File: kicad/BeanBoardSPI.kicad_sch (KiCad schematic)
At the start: 40 parts, among them J1 Power, J10 SPI6, J11 GPO, J12 GPO, J13 GPI, J14 GPI, J15 Power, J2 Address, J3 Data / Control, J4 SPI0 (RA8875), J5 SPI1, J6 SPI2, J7 SPI3, J8 SPI4, J9 SPI5, U1 74HC244, U10 74HC138, U11 74HC165, U12 74HC244, U13 74HC02, U2 74HC164, U3 74HC165, U4 74HC373, U5 74HC165, U6 74HC165, U8 74HC02, U9 74HC74

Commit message: schematic
tidy footprints  symbols
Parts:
- J1: value Power -> Conn_01x03_Pin
- J12: value GPO -> Conn_01x10_Pin
- J13: value GPI -> Conn_01x10_Pin
- J2: value Address -> Conn_01x16_Pin
- J3: value Data / Control -> Conn_01x16_Pin
- JP1: value CLK -> Jumper_2_Open; symbol Jumper:Jumper_2_Open -> PinHeader_Jumper:Jumper_2_Open
- JP2: value CLK/2 -> Jumper_2_Open; symbol Jumper:Jumper_2_Open -> PinHeader_Jumper:Jumper_2_Open
- JP3: symbol Jumper:Jumper_2_Bridged -> PinHeader_Jumper:Jumper_2_Bridged
- U1, U12: footprint (none) -> Package_DIP:DIP-20_W7.62mm
- U11, U3, U5, U6: footprint (none) -> Package_DIP:DIP-16_W7.62mm
- U13, U2: footprint (none) -> Package_DIP:DIP-14_W7.62mm_Socket
- U8: renamed from U13; footprint (none) -> Package_DIP:DIP-14_W7.62mm_Socket
- renumbered U8 to U13
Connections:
- net CTRL_WR: now also U13.10; no longer U13.13
- net INT_CLK: now also U13.12; no longer U13.3
- net SER_CLK: now also U13.13; no longer U13.1
- net ~{DATA_RD}: now also U8.4; no longer U8.10
- net ~{RD}: now also U8.2; no longer U8.5
- net ~{SER_EN}: now also U13.11; no longer U13.2
- net ~{WR}: now also U13.8; no longer U13.11
- net at U10.10 (~{Y5}), U8.8: now also U8.3; no longer U8.6
- net at U10.11 (~{Y4}), U13.3: now also U13.9; no longer U13.12
- new net: U8.1, U8.5, U8.6
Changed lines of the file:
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@@
 		(lib_id "74xx:74HC02")
 		(at 87.63 107.95 0)
-		(unit 2)
+		(unit 1)
 		(body_style 1)
 		(exclude_from_sim no)
@@
 				(path "/6c08ad2a-e233-4d4c-8add-9bc0e49a4487"
 					(reference "U8")
-					(unit 2)
+					(unit 1)
 				)
 			)
@@
 		(lib_id "74xx:74HC02")
 		(at 102.87 107.95 0)
-		(unit 3)
+		(unit 2)
 		(body_style 1)
 		(exclude_from_sim no)
@@
 		(in_pos_files yes)
 		(dnp no)
-		(fields_autoplaced yes)
-		(property "Reference" "U13"
-			(at 102.87 99.06 0)
+		(property "Reference" "U8"
+			(at 102.87 107.95 0)
 			(show_name no)
 			(do_not_autoplace no)
@@
 			)
 		)
-		(property "Footprint" ""
+		(property "Footprint" "Package_DIP:DIP-14_W7.62mm_Socket"
 			(at 102.87 107.95 0)
 			(hide yes)
@@
 			(project "BeanBoardSPI"
 				(path "/6c08ad2a-e233-4d4c-8add-9bc0e49a4487"
-					(reference "U13")
-					(unit 3)
+					(reference "U8")
+					(unit 2)
 				)
 			)
@@
 	)
 	(symbol
-		(lib_id "Jumper:Jumper_2_Open")
+		(lib_id "PinHeader_Jumper:Jumper_2_Open")
 		(at 163.83 149.86 0)
 		(unit 1)
@@
 		(dnp no)
 		(property "Reference" "JP1"
-			(at 163.6527 146.4748 0)
+			(at 163.83 147.066 0)
 			(show_name no)
 			(do_not_autoplace no)
@@
 			)
 		)
-		(property "Value" "CLK"
-			(at 163.83 146.05 0)
+		(property "Value" "Jumper_2_Open"
+			(at 163.83 152.146 0)
 			(hide yes)
 			(show_name no)
@@
 			)
 		)
-		(property "Description" ""
+		(property "Description" "Jumper, 2-pole, open"
 			(at 163.83 149.86 0)
+			(hide yes)
 			(show_name no)
 			(do_not_autoplace no)
@@
 			)
 		)
-		(property "Footprint" ""
+		(property "Footprint" "Package_DIP:DIP-16_W7.62mm"
 			(at 275.59 97.79 0)
 			(hide yes)
@@
 			)
 		)
-		(property "Footprint" ""
+		(property "Footprint" "Package_DIP:DIP-20_W7.62mm"
 			(at 223.52 95.25 0)
 			(hide yes)
@@
 			)
 		)
-		(property "Footprint" ""
+		(property "Footprint" "Package_DIP:DIP-16_W7.62mm"
 			(at 332.74 152.4 0)
 			(hide yes)
@@
 			)
 		)
-		(property "Footprint" ""
+		(property "Footprint" "Package_DIP:DIP-14_W7.62mm_Socket"
 			(at 11.43 160.02 0)
 			(hide yes)
@@
 		(in_pos_files yes)
 		(dnp no)
-		(fields_autoplaced yes)
 		(property "Reference" "U13"
-			(at 99.06 69.85 0)
+			(at 99.314 78.74 0)
 			(show_name no)
 			(do_not_autoplace no)
@@
 		(property "Value" "74HC02"
 			(at 99.06 72.39 0)
+			(hide yes)
 			(show_name no)
 			(do_not_autoplace no)
@@
 			)
 		)
-		(property "Footprint" ""
+		(property "Footprint" "Package_DIP:DIP-14_W7.62mm_Socket"
 			(at 99.06 78.74 0)
 			(hide yes)
@@
 			)
 		)
-		(property "Value" "Power"
+		(property "Value" "Conn_01x03_Pin"
 			(at 76.2 6.35 0)
+			(hide yes)
 			(show_name no)
 			(do_not_autoplace no)
@@
 			)
 		)
-		(property "Description" ""
+		(property "Description" "Generic connector, single row, 01x03, script generated"
 			(at 73.66 13.97 0)
+			(hide yes)
 			(show_name no)
 			(do_not_autoplace no)
@@
 		(in_pos_files yes)
 		(dnp no)
-		(fields_autoplaced yes)
 		(property "Reference" "U13"
-			(at 83.82 69.85 0)
+			(at 84.328 78.74 0)
 			(show_name no)
 			(do_not_autoplace no)
@@
 		(property "Value" "74HC02"
 			(at 83.82 72.39 0)
+			(hide yes)
 			(show_name no)
 			(do_not_autoplace no)
@@
 			)
 		)
-		(property "Footprint" ""
+		(property "Footprint" "Package_DIP:DIP-14_W7.62mm_Socket"
 			(at 83.82 78.74 0)
 			(hide yes)
@@
 		(in_pos_files yes)
 		(dnp no)
-		(fields_autoplaced yes)
-		(property "Reference" "U13"
-			(at 101.6 115.57 0)
+		(property "Reference" "U8"
+			(at 101.854 124.46 0)
 			(show_name no)
 			(do_not_autoplace no)
@@
 		(property "Value" "74HC02"
 			(at 101.6 118.11 0)
+			(hide yes)
 			(show_name no)
 			(do_not_autoplace no)
@@
 			)
 		)
-		(property "Footprint" ""
+		(property "Footprint" "Package_DIP:DIP-14_W7.62mm_Socket"
 			(at 101.6 124.46 0)
 			(hide yes)
@@
 			(project "BeanBoardSPI"
 				(path "/6c08ad2a-e233-4d4c-8add-9bc0e49a4487"
-					(reference "U13")
+					(reference "U8")
 					(unit 4)
 				)
@@
 			)
 		)
-		(property "Footprint" ""
+		(property "Footprint" "Package_DIP:DIP-14_W7.62mm_Socket"
 			(at 212.09 97.79 0)
 			(hide yes)
@@
 			)
 		)
-		(property "Footprint" ""
+		(property "Footprint" "Package_DIP:DIP-16_W7.62mm"
 			(at 332.74 97.79 0)
 			(hide yes)
@@
 		(lib_id "74xx:74HC02")
 		(at 93.98 90.17 0)
-		(unit 4)
+		(unit 3)
 		(body_style 1)
 		(exclude_from_sim no)
@@
 		(in_pos_files yes)
 		(dnp no)
-		(property "Reference" "U8"
+		(property "Reference" "U13"
 			(at 93.98 90.17 0)
 			(show_name no)
@@
 			(project "BeanBoardSPI"
 				(path "/6c08ad2a-e233-4d4c-8add-9bc0e49a4487"
-					(reference "U8")
-					(unit 4)
+					(reference "U13")
+					(unit 3)
 				)
 			)
@@
 	)
 	(symbol
-		(lib_id "Jumper:Jumper_2_Bridged")
+		(lib_id "PinHeader_Jumper:Jumper_2_Bridged")
 		(at 163.83 161.29 0)
 		(unit 1)
@@
 		(dnp no)
 		(property "Reference" "JP3"
-			(at 163.8593 159.3734 0)
+			(at 163.83 159.385 0)
 			(show_name no)
 			(do_not_autoplace no)
@@
 		)
 		(property "Value" "Jumper_2_Bridged"
-			(at 163.83 158.75 0)
+			(at 163.83 163.83 0)
 			(hide yes)
 			(show_name no)
@@
 		)
 		(property "Datasheet" ""
-			(at 163.83 161.29 0)
+			(at 163.83 166.37 0)
 			(hide yes)
 			(show_name no)
@@
 		)
 		(property "Description" "Jumper, 2-pole, closed/bridged"
-			(at 163.83 161.29 0)
+			(at 163.83 168.91 0)
 			(hide yes)
 			(show_name no)
@@
 			)
 		)
-		(property "Value" "Data / Control"
+		(property "Value" "Conn_01x16_Pin"
 			(at 55.88 8.89 0)
+			(hide yes)
 			(show_name no)
 			(do_not_autoplace no)
@@
 			)
 		)
-		(property "Description" ""
+		(property "Description" "Generic connector, single row, 01x16, script generated"
 			(at 55.88 31.75 0)
+			(hide yes)
 			(show_name no)
 			(do_not_autoplace no)
@@
 			)
 		)
-		(property "Footprint" ""
+		(property "Footprint" "Package_DIP:DIP-20_W7.62mm"
 			(at 223.52 146.05 0)
 			(hide yes)
@@
 		(lib_id "74xx:74HC02")
 		(at 176.53 142.24 0)
-		(unit 1)
+		(unit 4)
 		(body_style 1)
 		(exclude_from_sim no)
@@
 		(in_pos_files yes)
 		(dnp no)
-		(property "Reference" "U8"
+		(property "Reference" "U13"
 			(at 176.53 142.24 0)
 			(show_name no)
@@
 			(project "BeanBoardSPI"
 				(path "/6c08ad2a-e233-4d4c-8add-9bc0e49a4487"
-					(reference "U8")
-					(unit 1)
+					(reference "U13")
+					(unit 4)
 				)
 			)
@@
 			)
 		)
-		(property "Value" "GPO"
+		(property "Value" "Conn_01x10_Pin"
 			(at 74.93 24.13 0)
+			(hide yes)
 			(show_name no)
 			(do_not_autoplace no)
@@
 			)
 		)
-		(property "Description" ""
+		(property "Description" "Generic connector, single row, 01x10, script generated"
 			(at 73.66 38.1 0)
+			(hide yes)
 			(show_name no)
 			(do_not_autoplace no)
@@
 			)
 		)
-		(property "Value" "GPI"
+		(property "Value" "Conn_01x10_Pin"
 			(at 90.17 24.13 0)
+			(hide yes)
 			(show_name no)
 			(do_not_autoplace no)
@@
 			)
 		)
-		(property "Description" ""
+		(property "Description" "Generic connector, single row, 01x10, script generated"
 			(at 88.9 38.1 0)
+			(hide yes)
 			(show_name no)
 			(do_not_autoplace no)
@@
 			)
 		)
-		(property "Value" "Address"
+		(property "Value" "Conn_01x16_Pin"
 			(at 36.83 8.89 0)
+			(hide yes)
 			(show_name no)
 			(do_not_autoplace no)
@@
 			)
 		)
-		(property "Description" ""
+		(property "Description" "Generic connector, single row, 01x16, script generated"
 			(at 34.29 31.75 0)
+			(hide yes)
 			(show_name no)
 			(do_not_autoplace no)
@@
 	)
 	(symbol
-		(lib_id "Jumper:Jumper_2_Open")
+		(lib_id "PinHeader_Jumper:Jumper_2_Open")
 		(at 163.83 156.21 0)
 		(unit 1)
@@
 		(dnp no)
 		(property "Reference" "JP2"
-			(at 163.7904 153.2837 0)
+			(at 163.83 153.416 0)
 			(show_name no)
 			(do_not_autoplace no)
@@
 			)
 		)
-		(property "Value" "CLK/2"
-			(at 163.83 152.4 0)
+		(property "Value" "Jumper_2_Open"
+			(at 163.83 158.496 0)
 			(hide yes)
 			(show_name no)
@@
 			)
 		)
-		(property "Description" ""
+		(property "Description" "Jumper, 2-pole, open"
 			(at 163.83 156.21 0)
+			(hide yes)
 			(show_name no)
 			(do_not_autoplace no)
@@
 			)
 		)
-		(property "Footprint" ""
+		(property "Footprint" "Package_DIP:DIP-16_W7.62mm"
 			(at 275.59 152.4 0)
 			(hide yes)

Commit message: schematic
remove unused libraries
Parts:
- U1, U12: symbol 74xx:74HC244 -> 74HC244:74HC244
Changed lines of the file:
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@@
 	)
 	(symbol
-		(lib_id "74xx:74HC244")
+		(lib_id "74HC244:74HC244")
 		(at 223.52 95.25 0)
 		(unit 1)
@@
 		(dnp no)
 		(property "Reference" "U1"
-			(at 228.854 74.676 0)
-			(show_name no)
-			(do_not_autoplace no)
-			(effects
-				(font
-					(size 1.27 1.27)
-				)
-				(justify left)
+			(at 215.9 78.74 0)
+			(show_name no)
+			(do_not_autoplace no)
+			(effects
+				(font
+					(size 1.27 1.27)
+				)
 			)
 		)
 		(property "Value" "74HC244"
-			(at 225.6633 77.47 0)
-			(show_name no)
-			(do_not_autoplace no)
-			(effects
-				(font
-					(size 1.27 1.27)
-				)
-				(justify left)
+			(at 215.9 111.76 0)
+			(show_name no)
+			(do_not_autoplace no)
+			(effects
+				(font
+					(size 1.27 1.27)
+				)
 			)
 		)
@@
 	)
 	(symbol
-		(lib_id "74xx:74HC244")
+		(lib_id "74HC244:74HC244")
 		(at 223.52 146.05 0)
 		(unit 1)
@@
 		(dnp no)
 		(property "Reference" "U12"
-			(at 228.854 125.476 0)
-			(show_name no)
-			(do_not_autoplace no)
-			(effects
-				(font
-					(size 1.27 1.27)
-				)
-				(justify left)
+			(at 215.9 129.54 0)
+			(show_name no)
+			(do_not_autoplace no)
+			(effects
+				(font
+					(size 1.27 1.27)
+				)
 			)
 		)
 		(property "Value" "74HC244"
-			(at 225.6633 128.27 0)
-			(show_name no)
-			(do_not_autoplace no)
-			(effects
-				(font
-					(size 1.27 1.27)
-				)
-				(justify left)
-			)
-		)
+			(at 215.9 162.56 0)
+			(show_name no)
+			(do_not_autoplace no)
+			(effects
+				(font
+					(size 1.27 1.27)
+				)
+			)
+		)

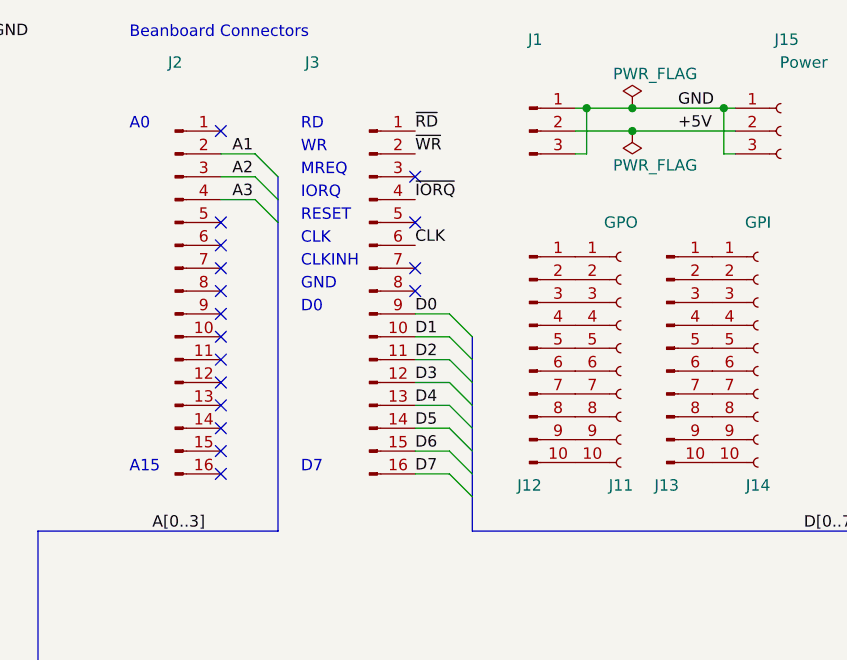
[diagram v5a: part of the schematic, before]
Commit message: schematic
update project libs
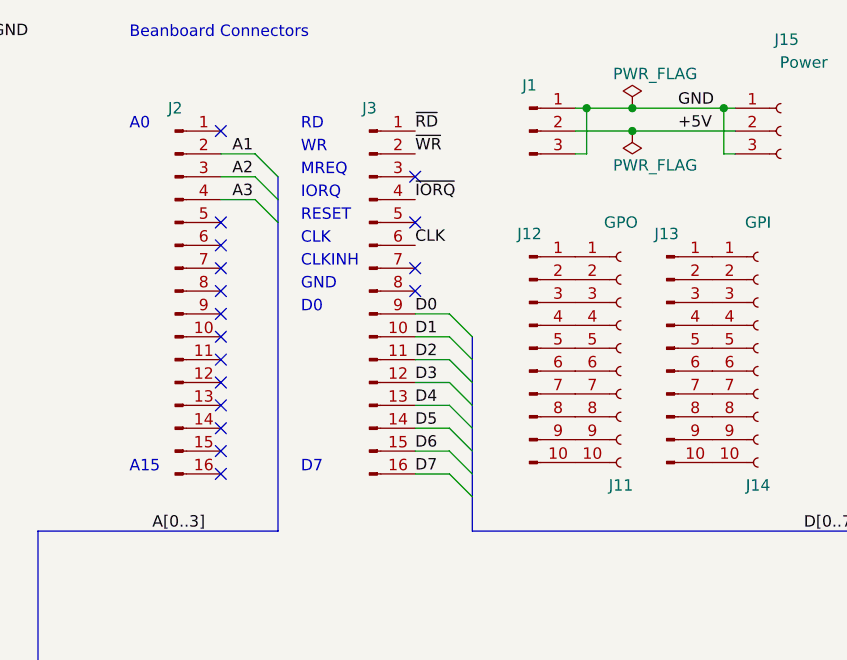
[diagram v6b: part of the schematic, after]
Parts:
- J1: footprint AltFootprints:PinHeader_1x03_P2.54mm_Vertical -> BeanBoardSPI:PinHeader_1x03_P2.54mm_Vertical; symbol Connector:Conn_01x03_Pin -> BeanBoardSPI:Conn_01x03_Pin
- J12, J13: footprint AltFootprints:PinHeader_1x10_P2.54mm_Vertical -> BeanBoardSPI:PinHeader_1x10_P2.54mm_Vertical; symbol Connector:Conn_01x10_Pin -> BeanBoardSPI:Conn_01x10_Pin
- J2, J3: footprint AltFootprints:PinHeader_1x16_P2.54mm_Vertical -> BeanBoardSPI:PinHeader_1x16_P2.54mm_Vertical; symbol Connector:Conn_01x16_Pin -> BeanBoardSPI:Conn_01x16_Pin
- JP1, JP2: symbol PinHeader_Jumper:Jumper_2_Open -> BeanBoardSPI:Jumper_2_Open
- JP3: symbol PinHeader_Jumper:Jumper_2_Bridged -> BeanBoardSPI:Jumper_2_Bridged
- U1, U12: symbol 74HC244:74HC244 -> BeanBoardSPI:74HC244
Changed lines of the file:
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@@
 	)
 	(symbol
-		(lib_id "PinHeader_Jumper:Jumper_2_Open")
+		(lib_id "BeanBoardSPI:Jumper_2_Open")
 		(at 163.83 149.86 0)
 		(unit 1)
@@
 	)
 	(symbol
-		(lib_id "74HC244:74HC244")
+		(lib_id "BeanBoardSPI:74HC244")
 		(at 223.52 95.25 0)
 		(unit 1)
@@
 	)
 	(symbol
-		(lib_id "Connector:Conn_01x03_Pin")
+		(lib_id "BeanBoardSPI:Conn_01x03_Pin")
 		(at 73.66 13.97 0)
 		(unit 1)
@@
 		(dnp no)
 		(property "Reference" "J1"
-			(at 74.295 3.81 0)
+			(at 73.66 8.89 0)
 			(show_name no)
 			(do_not_autoplace no)
@@
 		)
 		(property "Value" "Conn_01x03_Pin"
-			(at 76.2 6.35 0)
+			(at 73.66 19.05 0)
 			(hide yes)
 			(show_name no)
@@
 			)
 		)
-		(property "Footprint" "AltFootprints:PinHeader_1x03_P2.54mm_Vertical"
+		(property "Footprint" "BeanBoardSPI:PinHeader_1x03_P2.54mm_Vertical"
 			(at 73.66 13.97 0)
 			(hide yes)
@@
 	)
 	(symbol
-		(lib_id "PinHeader_Jumper:Jumper_2_Bridged")
+		(lib_id "BeanBoardSPI:Jumper_2_Bridged")
 		(at 163.83 161.29 0)
 		(unit 1)
@@
 	)
 	(symbol
-		(lib_id "Connector:Conn_01x16_Pin")
+		(lib_id "BeanBoardSPI:Conn_01x16_Pin")
 		(at 55.88 31.75 0)
 		(unit 1)
@@
 		(dnp no)
 		(property "Reference" "J3"
-			(at 49.53 6.35 0)
+			(at 55.88 11.43 0)
 			(show_name no)
 			(do_not_autoplace no)
@@
 		)
 		(property "Value" "Conn_01x16_Pin"
-			(at 55.88 8.89 0)
+			(at 55.88 54.61 0)
 			(hide yes)
 			(show_name no)
@@
 			)
 		)
-		(property "Footprint" "AltFootprints:PinHeader_1x16_P2.54mm_Vertical"
+		(property "Footprint" "BeanBoardSPI:PinHeader_1x16_P2.54mm_Vertical"
 			(at 55.88 31.75 0)
 			(hide yes)
@@
 	)
 	(symbol
-		(lib_id "74HC244:74HC244")
+		(lib_id "BeanBoardSPI:74HC244")
 		(at 223.52 146.05 0)
 		(unit 1)
@@
 	)
 	(symbol
-		(lib_id "Connector:Conn_01x10_Pin")
+		(lib_id "BeanBoardSPI:Conn_01x10_Pin")
 		(at 73.66 38.1 0)
 		(unit 1)
@@
 		(dnp no)
 		(property "Reference" "J12"
-			(at 73.66 53.34 0)
+			(at 73.66 25.4 0)
 			(show_name no)
 			(do_not_autoplace no)
@@
 		)
 		(property "Value" "Conn_01x10_Pin"
-			(at 74.93 24.13 0)
+			(at 73.66 53.34 0)
 			(hide yes)
 			(show_name no)
@@
 			)
 		)
-		(property "Footprint" "AltFootprints:PinHeader_1x10_P2.54mm_Vertical"
+		(property "Footprint" "BeanBoardSPI:PinHeader_1x10_P2.54mm_Vertical"
 			(at 73.66 38.1 0)
 			(hide yes)
@@
 	)
 	(symbol
-		(lib_id "Connector:Conn_01x10_Pin")
+		(lib_id "BeanBoardSPI:Conn_01x10_Pin")
 		(at 88.9 38.1 0)
 		(unit 1)
@@
 		(dnp no)
 		(property "Reference" "J13"
-			(at 88.9 53.34 0)
+			(at 88.9 25.4 0)
 			(show_name no)
 			(do_not_autoplace no)
@@
 		)
 		(property "Value" "Conn_01x10_Pin"
-			(at 90.17 24.13 0)
+			(at 88.9 53.34 0)
 			(hide yes)
 			(show_name no)
@@
 			)
 		)
-		(property "Footprint" "AltFootprints:PinHeader_1x10_P2.54mm_Vertical"
+		(property "Footprint" "BeanBoardSPI:PinHeader_1x10_P2.54mm_Vertical"
 			(at 88.9 38.1 0)
 			(hide yes)
@@
 	)
 	(symbol
-		(lib_id "Connector:Conn_01x16_Pin")
+		(lib_id "BeanBoardSPI:Conn_01x16_Pin")
 		(at 34.29 31.75 0)
 		(unit 1)
@@
 		(dnp no)
 		(property "Reference" "J2"
-			(at 34.29 6.35 0)
+			(at 34.29 11.43 0)
 			(show_name no)
 			(do_not_autoplace no)
@@
 		)
 		(property "Value" "Conn_01x16_Pin"
-			(at 36.83 8.89 0)
+			(at 34.29 54.61 0)
 			(hide yes)
 			(show_name no)
@@
 			)
 		)
-		(property "Footprint" "AltFootprints:PinHeader_1x16_P2.54mm_Vertical"
+		(property "Footprint" "BeanBoardSPI:PinHeader_1x16_P2.54mm_Vertical"
 			(at 34.29 31.75 0)
 			(hide yes)
@@
 	)
 	(symbol
-		(lib_id "PinHeader_Jumper:Jumper_2_Open")
+		(lib_id "BeanBoardSPI:Jumper_2_Open")
 		(at 163.83 156.21 0)
 		(unit 1)
